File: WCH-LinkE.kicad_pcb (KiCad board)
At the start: 2 copper layers, 38.1 x 17.8 mm, 35 parts, among them J2 Conn_02x05_Odd_Even, J3 USB_C_Receptacle_USB2.0_16P, SW1 SW_Push, SW2 SW_Push, U1 AMS1117-3.3, U2 CH32V305FBP6, U3 CH217K, U4 CH217K, Y2 12M

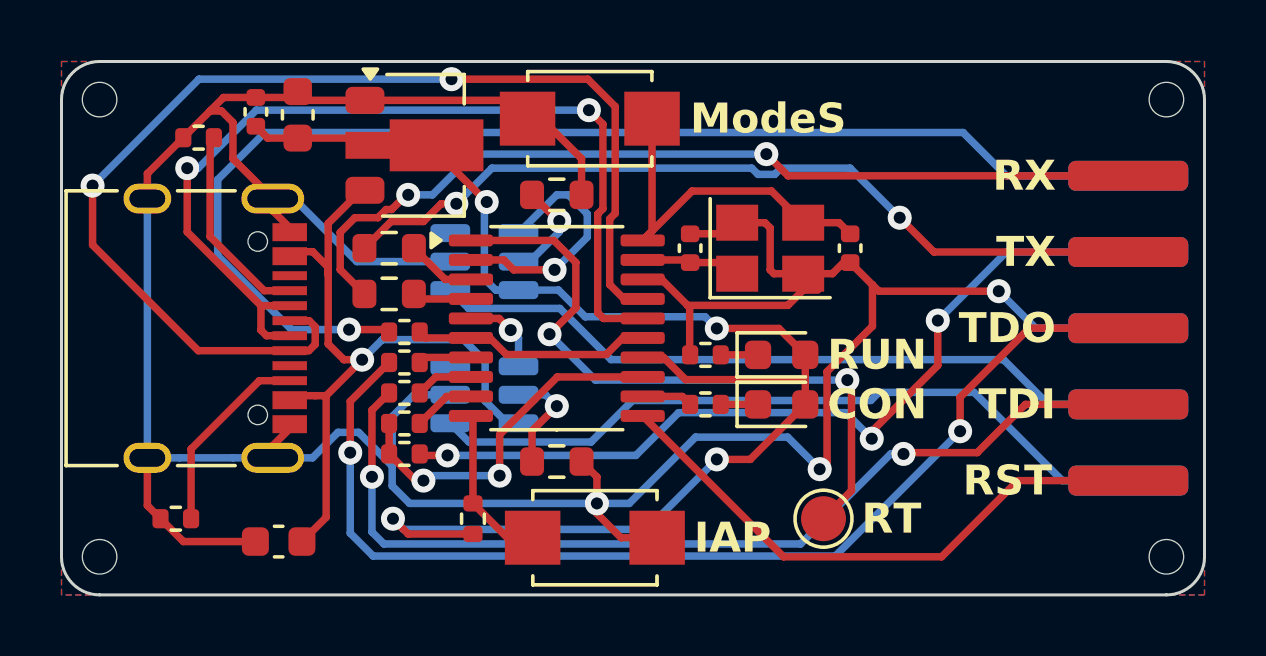
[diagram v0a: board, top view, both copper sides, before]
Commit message: csv position fix
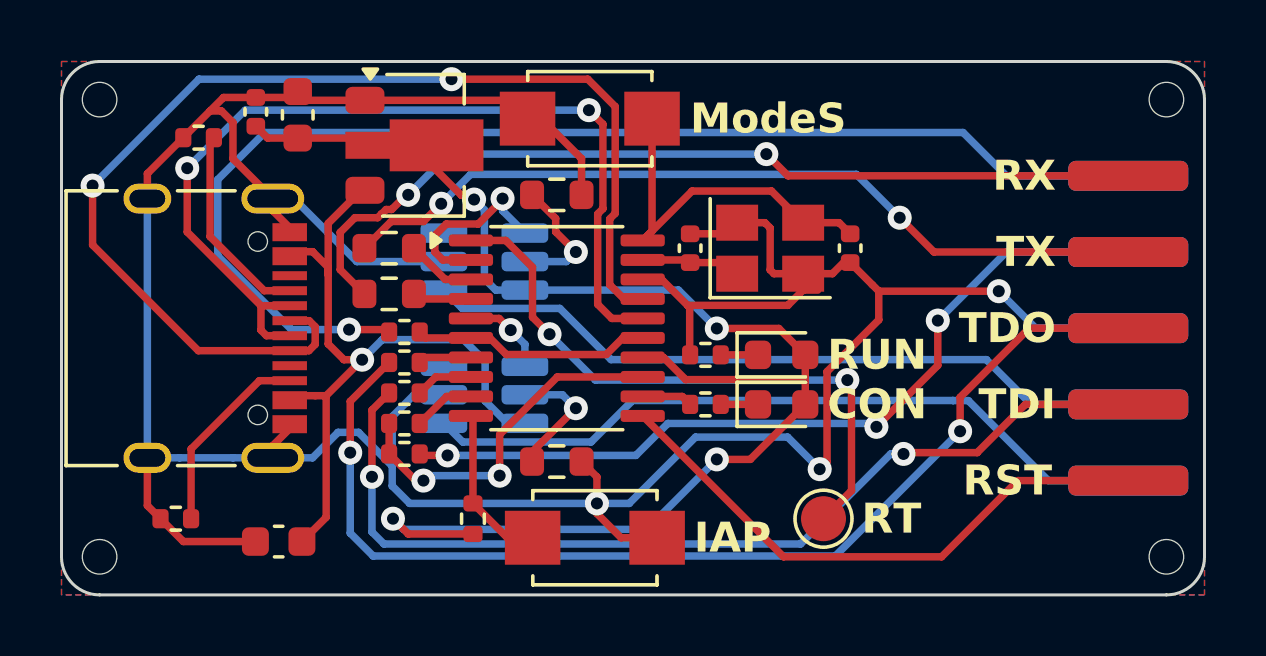
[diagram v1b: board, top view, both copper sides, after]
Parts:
- U3, U4: footprint Package_TO_SOT_SMD:SOT-23-6 -> Package_TO_SOT_SMD:SOT-23-6_Handsoldering
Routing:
- net /PA5: track 8.32 -> 6.11 mm
- net Net-(U2-~{RST}): track 22.2 -> 20.5 mm
- net Net-(U4-ISET): track 3.40 -> 4.34 mm
- net Net-(U3-ISET): track 3.62 -> 4.48 mm
- net /SWDIO/TMS: track 28.2 -> 27.4 mm

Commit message: move ch217k
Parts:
- C2: value 10u -> 1u; footprint Capacitor_SMD:C_0603_1608Metric -> Capacitor_SMD:C_0402_1005Metric
- C4: value 22u -> 10u; footprint Capacitor_SMD:C_0603_1608Metric -> Capacitor_SMD:C_0402_1005Metric
- U1: value AMS1117-3.3 -> RT9080-33GJ5; footprint Package_TO_SOT_SMD:SOT-89-3 -> Package_TO_SOT_SMD:TSOT-23-5
- U3, U4: footprint Package_TO_SOT_SMD:SOT-23-6_Handsoldering -> Package_TO_SOT_SMD:SOT-23-6; moved to F.Cu
- moved C5 23.6 mm to (154.3, 121.9), turned to 0 degrees
- moved U3 13.9 mm to (154.3, 124.7), turned to 180 degrees
- moved U4 13.9 mm to (154.3, 111.5), turned to 180 degrees
- moved C2 13.2 mm to (140.6, 113.7), turned to 0 degrees
- moved TP1 4.10 mm to (148.6, 122.9)
- moved SW2 1.27 mm to (143.5, 125.1)
- moved U1 1.20 mm to (138.0, 111.4), turned to 180 degrees
- moved SW1 1.10 mm to (143.5, 111.1)
- moved R10 1.02 mm to (139.7, 124.5)
- moved R12 0.63 mm to (131.4, 124.5)
- moved C4 0.13 mm to (134.9, 110.9)
- moved R11 0.12 mm to (131.4, 111.8)
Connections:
- U1 pad 1: GND -> +5V
- U1 pad 2: +3V3 -> GND
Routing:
- net +5V: track 25.1 -> 56.8 mm, vias 1 -> 3
- net GND: track 111.7 -> 142.0 mm, vias 3 -> 1
- net /USB_P: track 39.0 -> 18.8 mm
- net /5V_OUT: track 24.8 -> 8.14 mm, vias 0 -> 1
- net /PB12: track 2.89 -> 19.0 mm, vias 1 -> 2
- net /USB_N: track 31.0 -> 15.1 mm
- net +3V3: track 48.7 -> 64.6 mm
- net /PA5: track 6.11 -> 17.7 mm, vias 1 -> 2
- net /3V3_OUT: track 24.4 -> 13.3 mm, vias 0 -> 1
- net Net-(U4-ISET): track 4.34 -> 14.7 mm, vias 1 -> 0
- net /SWCLK/TCK: track 40.9 -> 32.4 mm
- net Net-(U3-ISET): track 4.48 -> 12.2 mm, vias 1 -> 0
- net Net-(U2-~{RST}): track 20.5 -> 13.4 mm
- net /TDO: track 36.3 -> 31.1 mm
- net /TDI: track 32.2 -> 29.9 mm
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
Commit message: position fix
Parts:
- J3: footprint Connector_USB:USB_C_Receptacle_XKB_U262-16XN-4BVC11 -> Connector_USB:USB_C_Receptacle_G-Switch_GT-USB-7010ASV

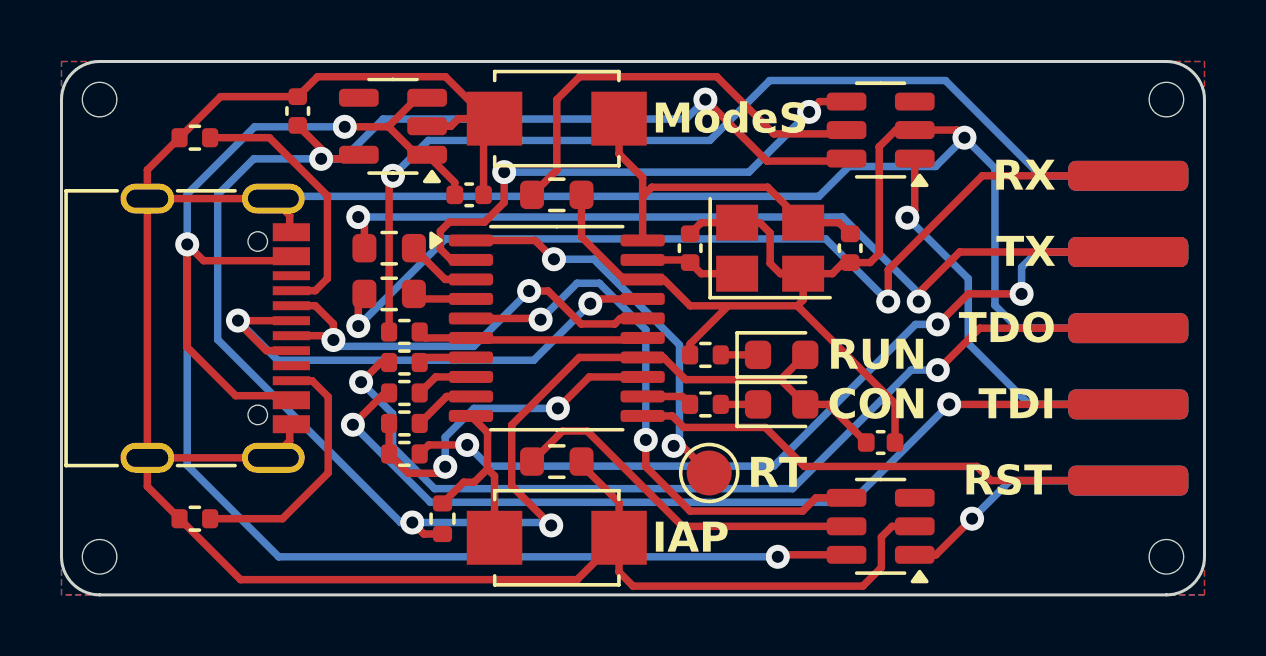
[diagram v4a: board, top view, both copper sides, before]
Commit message: fix trace width
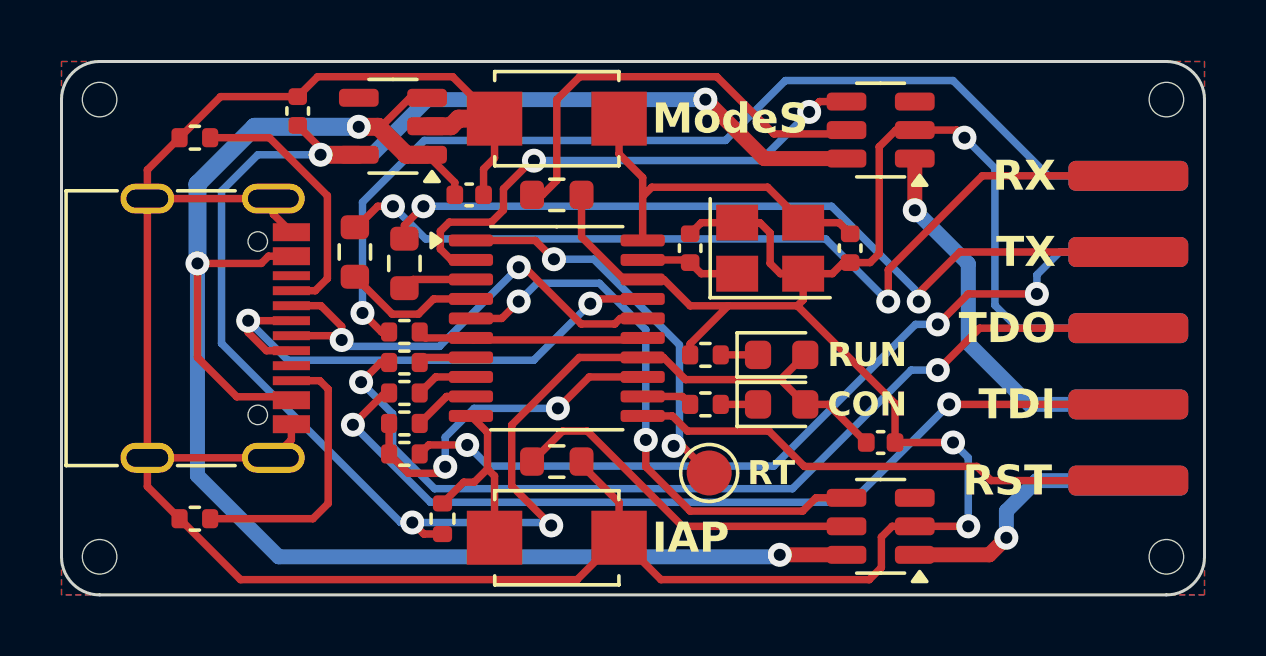
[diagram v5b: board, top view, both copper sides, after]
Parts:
- moved R3 1.81 mm to (136.8, 115.6), turned to 90 degrees
- moved R4 0.72 mm to (138.4, 116.0), turned to 90 degrees
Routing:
- net GND: track 142.0 -> 123.7 mm, vias 1 -> 3
- net Net-(U2-PB11): track 1.97 -> 4.60 mm
- net /TX: track 29.0 -> 27.2 mm
- net /RX: track 31.2 -> 29.7 mm
- net +5V: track 56.8 -> 55.8 mm
- net /SWCLK/TCK: track 32.4 -> 33.4 mm
- net /USB_N: track 15.5 -> 16.3 mm
- net /USB_P: track 18.8 -> 18.0 mm
- net Net-(J3-CC2): track 8.61 -> 9.36 mm
- net /5V_OUT: track 8.14 -> 8.66 mm

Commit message: fix trace for gnd
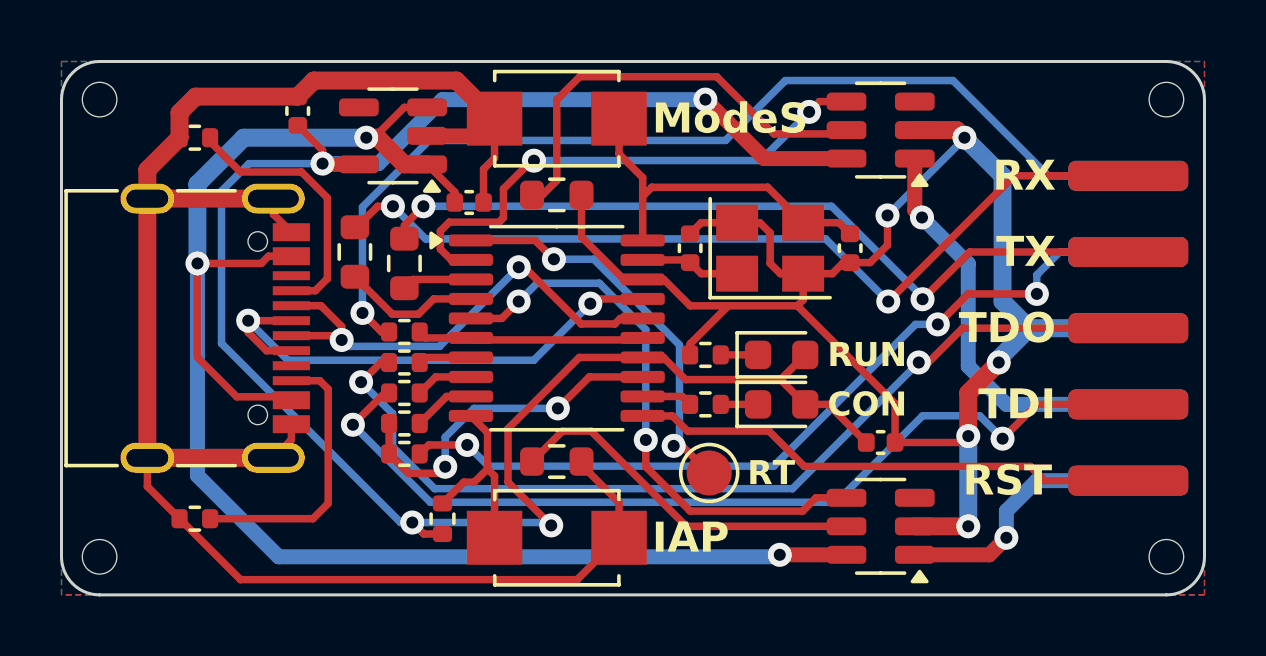
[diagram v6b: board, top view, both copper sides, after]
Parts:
- R11, R12: value 5.1kΩ -> 5.1k
- moved U1 0.32 mm to (138.0, 111.7)
- moved C2 0.25 mm to (140.6, 113.9)
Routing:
- net GND: track 123.7 -> 117.6 mm, vias 3 -> 5
- net /TDI: track 29.9 -> 30.5 mm
- net /RX: track 29.7 -> 29.1 mm

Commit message: optimize
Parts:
- moved R3 0.40 mm to (136.9, 116.0)

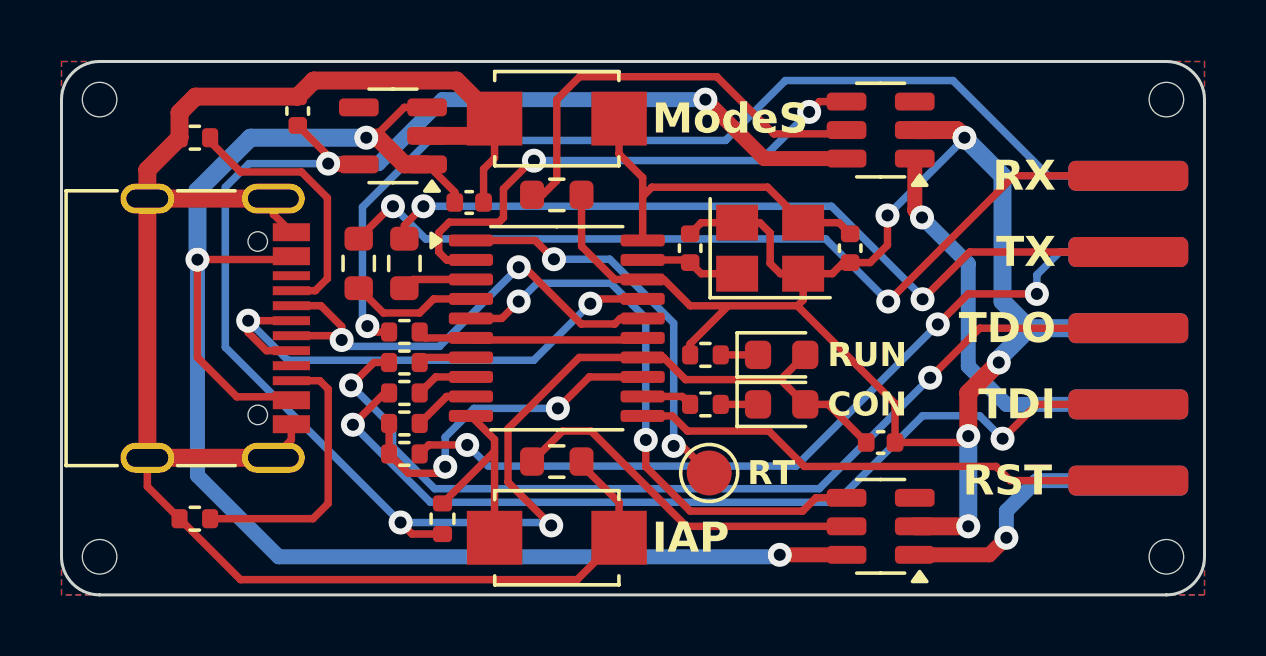
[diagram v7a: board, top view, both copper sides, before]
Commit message: fix button footprint
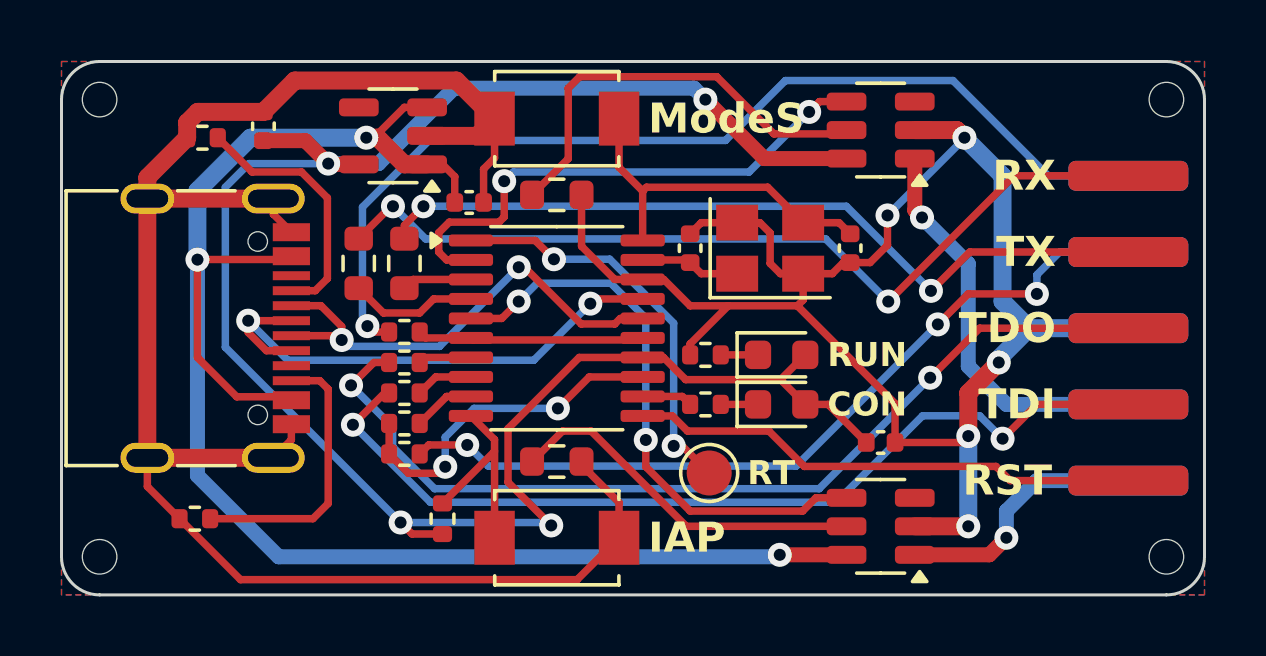
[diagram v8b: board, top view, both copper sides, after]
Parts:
- moved C4 1.25 mm to (133.7, 111.4)
- moved R11 0.25 mm to (131.7, 111.8)
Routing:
- net +3V3: track 64.8 -> 66.1 mm
